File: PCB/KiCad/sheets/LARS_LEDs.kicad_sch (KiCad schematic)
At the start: 26 parts, among them J29 LED1, J30 LED2, SW2 User Button

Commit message: reannotate schematic
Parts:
- renumbered C66 to C68, C67 to C69, C68 to C70, J29 to J30, J30 to J31
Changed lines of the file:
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@@
 		(dnp no)
 		(fields_autoplaced yes)
-		(property "Reference" "#PWR0196"
+		(property "Reference" "#PWR0193"
 			(at 232.41 72.39 0)
 			(effects
@@
 			(project "hardware_interface"
 				(path "/ffedf44c-a51a-4124-b6d3-e3f1f256e9ac/1e19cc26-d5ec-4418-898d-5c13f17cd2aa"
-					(reference "#PWR0196")
+					(reference "#PWR0193")
 					(unit 1)
 				)
@@
 		(on_board yes)
 		(dnp no)
-		(property "Reference" "C68"
+		(property "Reference" "C70"
 			(at 150.114 137.922 0)
 			(effects
@@
 			(project "hardware_interface"
 				(path "/ffedf44c-a51a-4124-b6d3-e3f1f256e9ac/1e19cc26-d5ec-4418-898d-5c13f17cd2aa"
-					(reference "C68")
+					(reference "C70")
 					(unit 1)
 				)
@@
 		(on_board yes)
 		(dnp no)
-		(property "Reference" "C66"
+		(property "Reference" "C68"
 			(at 232.664 59.182 0)
 			(effects
@@
 			(project "hardware_interface"
 				(path "/ffedf44c-a51a-4124-b6d3-e3f1f256e9ac/1e19cc26-d5ec-4418-898d-5c13f17cd2aa"
-					(reference "C66")
+					(reference "C68")
 					(unit 1)
 				)
@@
 		(dnp no)
 		(fields_autoplaced yes)
-		(property "Reference" "#PWR0189"
+		(property "Reference" "#PWR0186"
 			(at 106.68 50.8 0)
 			(effects
@@
 			(project "hardware_interface"
 				(path "/ffedf44c-a51a-4124-b6d3-e3f1f256e9ac/1e19cc26-d5ec-4418-898d-5c13f17cd2aa"
-					(reference "#PWR0189")
+					(reference "#PWR0186")
 					(unit 1)
 				)
@@
 		(dnp no)
 		(fields_autoplaced yes)
-		(property "Reference" "#PWR0199"
+		(property "Reference" "#PWR0196"
 			(at 137.16 73.66 0)
 			(effects
@@
 			(project "hardware_interface"
 				(path "/ffedf44c-a51a-4124-b6d3-e3f1f256e9ac/1e19cc26-d5ec-4418-898d-5c13f17cd2aa"
-					(reference "#PWR0199")
+					(reference "#PWR0196")
 					(unit 1)
 				)
@@
 		(dnp no)
 		(fields_autoplaced yes)
-		(property "Reference" "#PWR0197"
+		(property "Reference" "#PWR0194"
 			(at 106.68 73.66 0)
 			(effects
@@
 			(project "hardware_interface"
 				(path "/ffedf44c-a51a-4124-b6d3-e3f1f256e9ac/1e19cc26-d5ec-4418-898d-5c13f17cd2aa"
-					(reference "#PWR0197")
+					(reference "#PWR0194")
 					(unit 1)
 				)
@@
 		(dnp no)
 		(fields_autoplaced yes)
-		(property "Reference" "#PWR0193"
+		(property "Reference" "#PWR0190"
 			(at 46.99 72.39 0)
 			(effects
@@
 			(project "hardware_interface"
 				(path "/ffedf44c-a51a-4124-b6d3-e3f1f256e9ac/1e19cc26-d5ec-4418-898d-5c13f17cd2aa"
-					(reference "#PWR0193")
+					(reference "#PWR0190")
 					(unit 1)
 				)
@@
 		(on_board yes)
 		(dnp no)
-		(property "Reference" "#PWR0205"
+		(property "Reference" "#PWR0202"
 			(at 143.51 133.35 0)
 			(effects
@@
 			(project "hardware_interface"
 				(path "/ffedf44c-a51a-4124-b6d3-e3f1f256e9ac/1e19cc26-d5ec-4418-898d-5c13f17cd2aa"
-					(reference "#PWR0205")
+					(reference "#PWR0202")
 					(unit 1)
 				)
@@
 		(on_board yes)
 		(dnp no)
-		(property "Reference" "C67"
+		(property "Reference" "C69"
 			(at 143.764 137.922 0)
 			(effects
@@
 			(project "hardware_interface"
 				(path "/ffedf44c-a51a-4124-b6d3-e3f1f256e9ac/1e19cc26-d5ec-4418-898d-5c13f17cd2aa"
-					(reference "C67")
+					(reference "C69")
 					(unit 1)
 				)
@@
 		(on_board yes)
 		(dnp no)
-		(property "Reference" "J30"
+		(property "Reference" "J31"
 			(at 120.142 134.366 0)
 			(effects
@@
 			(project "hardware_interface"
 				(path "/ffedf44c-a51a-4124-b6d3-e3f1f256e9ac/1e19cc26-d5ec-4418-898d-5c13f17cd2aa"
-					(reference "J30")
+					(reference "J31")
 					(unit 1)
 				)
@@
 		(on_board yes)
 		(dnp no)
-		(property "Reference" "J29"
+		(property "Reference" "J30"
 			(at 66.802 134.366 0)
 			(effects
@@
 			(project "hardware_interface"
 				(path "/ffedf44c-a51a-4124-b6d3-e3f1f256e9ac/1e19cc26-d5ec-4418-898d-5c13f17cd2aa"
-					(reference "J29")
+					(reference "J30")
 					(unit 1)
 				)
@@
 		(dnp no)
 		(fields_autoplaced yes)
-		(property "Reference" "#PWR0210"
+		(property "Reference" "#PWR0207"
 			(at 143.51 157.48 0)
 			(effects
@@
 			(project "hardware_interface"
 				(path "/ffedf44c-a51a-4124-b6d3-e3f1f256e9ac/1e19cc26-d5ec-4418-898d-5c13f17cd2aa"
-					(reference "#PWR0210")
+					(reference "#PWR0207")
 					(unit 1)
 				)
@@
 		(dnp no)
 		(fields_autoplaced yes)
-		(property "Reference" "#PWR0203"
+		(property "Reference" "#PWR0200"
 			(at 62.23 133.35 0)
 			(effects
@@
 			(project "hardware_interface"
 				(path "/ffedf44c-a51a-4124-b6d3-e3f1f256e9ac/1e19cc26-d5ec-4418-898d-5c13f17cd2aa"
-					(reference "#PWR0203")
+					(reference "#PWR0200")
 					(unit 1)
 				)
@@
 		(dnp no)
 		(fields_autoplaced yes)
-		(property "Reference" "#PWR0188"
+		(property "Reference" "#PWR0185"
 			(at 232.41 43.18 0)
 			(effects
@@
 			(project "hardware_interface"
 				(path "/ffedf44c-a51a-4124-b6d3-e3f1f256e9ac/1e19cc26-d5ec-4418-898d-5c13f17cd2aa"
-					(reference "#PWR0188")
+					(reference "#PWR0185")
 					(unit 1)
 				)
@@
 		(dnp no)
 		(fields_autoplaced yes)
-		(property "Reference" "#PWR0202"
+		(property "Reference" "#PWR0199"
 			(at 99.06 123.19 0)
 			(effects
@@
 			(project "hardware_interface"
 				(path "/ffedf44c-a51a-4124-b6d3-e3f1f256e9ac/1e19cc26-d5ec-4418-898d-5c13f17cd2aa"
-					(reference "#PWR0202")
+					(reference "#PWR0199")
 					(unit 1)
 				)
@@
 		(dnp no)
 		(fields_autoplaced yes)
-		(property "Reference" "#PWR0200"
+		(property "Reference" "#PWR0197"
 			(at 196.85 73.66 0)
 			(effects
@@
 			(project "hardware_interface"
 				(path "/ffedf44c-a51a-4124-b6d3-e3f1f256e9ac/1e19cc26-d5ec-4418-898d-5c13f17cd2aa"
-					(reference "#PWR0200")
+					(reference "#PWR0197")
 					(unit 1)
 				)
@@
 		(dnp no)
 		(fields_autoplaced yes)
-		(property "Reference" "#PWR0195"
+		(property "Reference" "#PWR0192"
 			(at 67.31 72.39 0)
 			(effects
@@
 			(project "hardware_interface"
 				(path "/ffedf44c-a51a-4124-b6d3-e3f1f256e9ac/1e19cc26-d5ec-4418-898d-5c13f17cd2aa"
-					(reference "#PWR0195")
+					(reference "#PWR0192")
 					(unit 1)
 				)
@@
 		(dnp no)
 		(fields_autoplaced yes)
-		(property "Reference" "#PWR0198"
+		(property "Reference" "#PWR0195"
 			(at 121.92 73.66 0)
 			(effects
@@
 			(project "hardware_interface"
 				(path "/ffedf44c-a51a-4124-b6d3-e3f1f256e9ac/1e19cc26-d5ec-4418-898d-5c13f17cd2aa"
-					(reference "#PWR0198")
+					(reference "#PWR0195")
 					(unit 1)
 				)
@@
 		(dnp no)
 		(fields_autoplaced yes)
-		(property "Reference" "#PWR0204"
+		(property "Reference" "#PWR0201"
 			(at 115.57 133.35 0)
 			(effects
@@
 			(project "hardware_interface"
 				(path "/ffedf44c-a51a-4124-b6d3-e3f1f256e9ac/1e19cc26-d5ec-4418-898d-5c13f17cd2aa"
-					(reference "#PWR0204")
+					(reference "#PWR0201")
 					(unit 1)
 				)
@@
 		(dnp no)
 		(fields_autoplaced yes)
-		(property "Reference" "#PWR0201"
+		(property "Reference" "#PWR0198"
 			(at 45.72 123.19 0)
 			(effects
@@
 			(project "hardware_interface"
 				(path "/ffedf44c-a51a-4124-b6d3-e3f1f256e9ac/1e19cc26-d5ec-4418-898d-5c13f17cd2aa"
-					(reference "#PWR0201")
+					(reference "#PWR0198")
 					(unit 1)
 				)
@@
 		(dnp no)
 		(fields_autoplaced yes)
-		(property "Reference" "#PWR0191"
+		(property "Reference" "#PWR0188"
 			(at 137.16 50.8 0)
 			(effects
@@
 			(project "hardware_interface"
 				(path "/ffedf44c-a51a-4124-b6d3-e3f1f256e9ac/1e19cc26-d5ec-4418-898d-5c13f17cd2aa"
-					(reference "#PWR0191")
+					(reference "#PWR0188")
 					(unit 1)
 				)
@@
 		(dnp no)
 		(fields_autoplaced yes)
-		(property "Reference" "#PWR0194"
+		(property "Reference" "#PWR0191"
 			(at 57.15 72.39 0)
 			(effects
@@
 			(project "hardware_interface"
 				(path "/ffedf44c-a51a-4124-b6d3-e3f1f256e9ac/1e19cc26-d5ec-4418-898d-5c13f17cd2aa"
-					(reference "#PWR0194")
+					(reference "#PWR0191")
 					(unit 1)
 				)
@@
 		(dnp no)
 		(fields_autoplaced yes)
-		(property "Reference" "#PWR0208"
+		(property "Reference" "#PWR0205"
 			(at 99.06 157.48 0)
 			(effects
@@
 			(project "hardware_interface"
 				(path "/ffedf44c-a51a-4124-b6d3-e3f1f256e9ac/1e19cc26-d5ec-4418-898d-5c13f17cd2aa"
-					(reference "#PWR0208")
+					(reference "#PWR0205")
 					(unit 1)
 				)
@@
 		(dnp no)
 		(fields_autoplaced yes)
-		(property "Reference" "#PWR0206"
+		(property "Reference" "#PWR0203"
 			(at 45.72 157.48 0)
 			(effects
@@
 			(project "hardware_interface"
 				(path "/ffedf44c-a51a-4124-b6d3-e3f1f256e9ac/1e19cc26-d5ec-4418-898d-5c13f17cd2aa"
-					(reference "#PWR0206")
+					(reference "#PWR0203")
 					(unit 1)
 				)
@@
 		(dnp no)
 		(fields_autoplaced yes)
-		(property "Reference" "#PWR0192"
+		(property "Reference" "#PWR0189"
 			(at 158.75 50.8 0)
 			(effects
@@
 			(project "hardware_interface"
 				(path "/ffedf44c-a51a-4124-b6d3-e3f1f256e9ac/1e19cc26-d5ec-4418-898d-5c13f17cd2aa"
-					(reference "#PWR0192")
+					(reference "#PWR0189")
 					(unit 1)
 				)
@@
 		(dnp no)
 		(fields_autoplaced yes)
-		(property "Reference" "#PWR0209"
+		(property "Reference" "#PWR0206"
 			(at 115.57 157.48 0)
 			(effects
@@
 			(project "hardware_interface"
 				(path "/ffedf44c-a51a-4124-b6d3-e3f1f256e9ac/1e19cc26-d5ec-4418-898d-5c13f17cd2aa"
-					(reference "#PWR0209")
+					(reference "#PWR0206")
 					(unit 1)
 				)
@@
 		(dnp no)
 		(fields_autoplaced yes)
-		(property "Reference" "#PWR0207"
+		(property "Reference" "#PWR0204"
 			(at 62.23 157.48 0)
 			(effects
@@
 			(project "hardware_interface"
 				(path "/ffedf44c-a51a-4124-b6d3-e3f1f256e9ac/1e19cc26-d5ec-4418-898d-5c13f17cd2aa"
-					(reference "#PWR0207")
+					(reference "#PWR0204")
 					(unit 1)
 				)
@@
 		(on_board yes)
 		(dnp no)
-		(property "Reference" "#PWR0190"
+		(property "Reference" "#PWR0187"
 			(at 121.92 50.8 0)
 			(effects
@@
 			(project "hardware_interface"
 				(path "/ffedf44c-a51a-4124-b6d3-e3f1f256e9ac/1e19cc26-d5ec-4418-898d-5c13f17cd2aa"
-					(reference "#PWR0190")
+					(reference "#PWR0187")
 					(unit 1)
 				)

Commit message: add final traces
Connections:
- net +5V: no longer D16.2 (A), D17.2 (A)
- net +5V_OUT: now also D16.2 (A), D17.2 (A)
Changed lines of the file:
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@@
 			)
 		)
-		(property "Value" "+5V"
+		(property "Value" "+5V_OUT"
 			(at 99.06 114.3 0)
 			(effects
@@
 			)
 		)
-		(property "Value" "+5V"
+		(property "Value" "+5V_OUT"
 			(at 45.72 114.3 0)
 			(effects

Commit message: finish PCB routing
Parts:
- C68: value 1u -> 2u2
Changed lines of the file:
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@@
 			)
 		)
-		(property "Value" "1u"
+		(property "Value" "2u2"
 			(at 232.918 62.992 0)
 			(effects

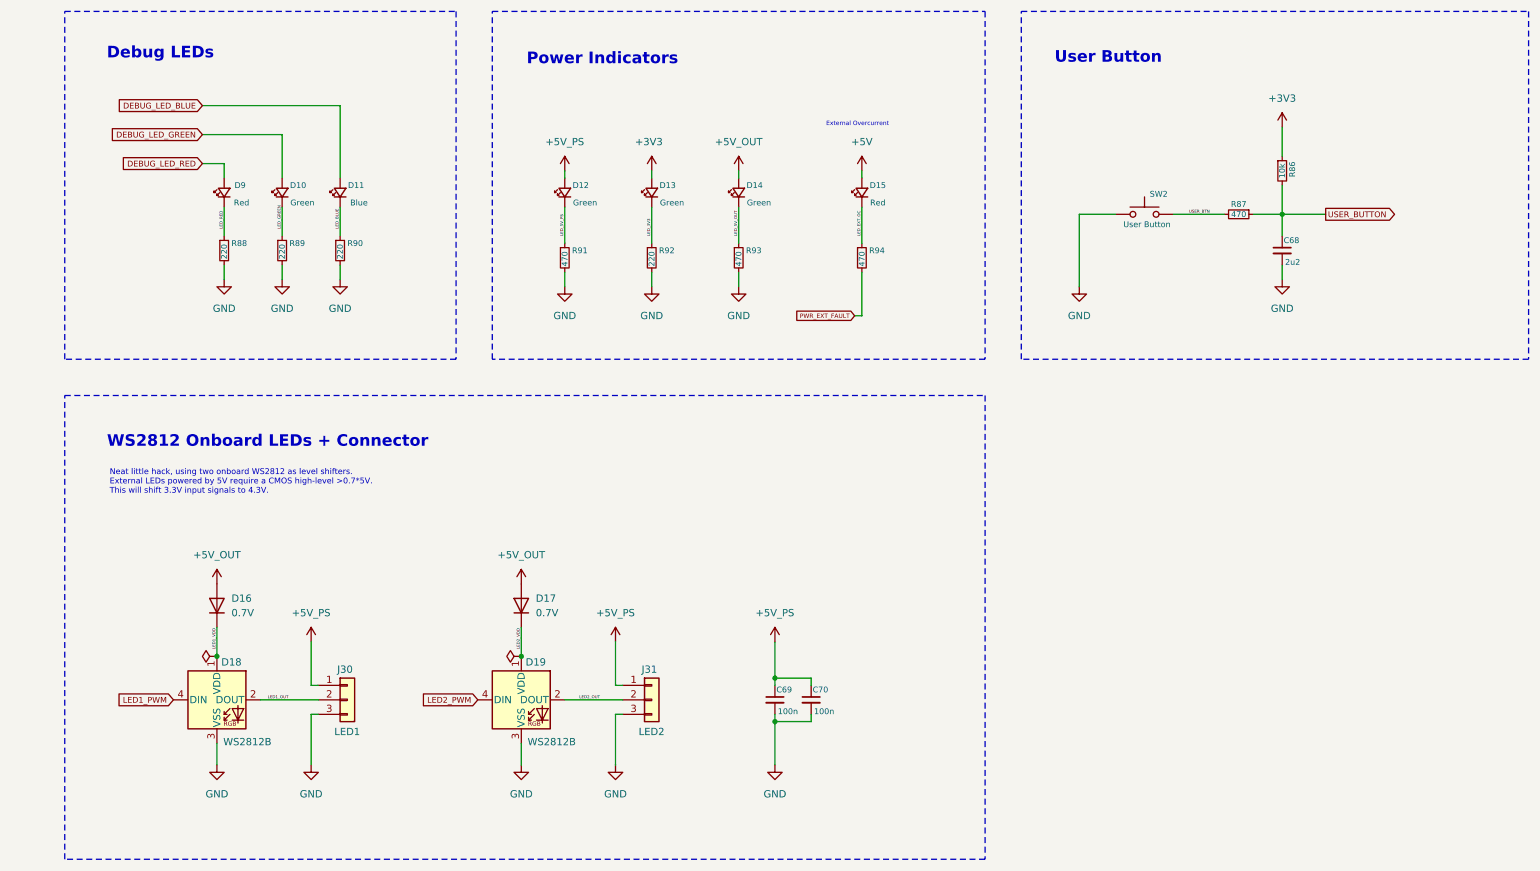
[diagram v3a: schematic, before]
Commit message: change default KiCad schematic font
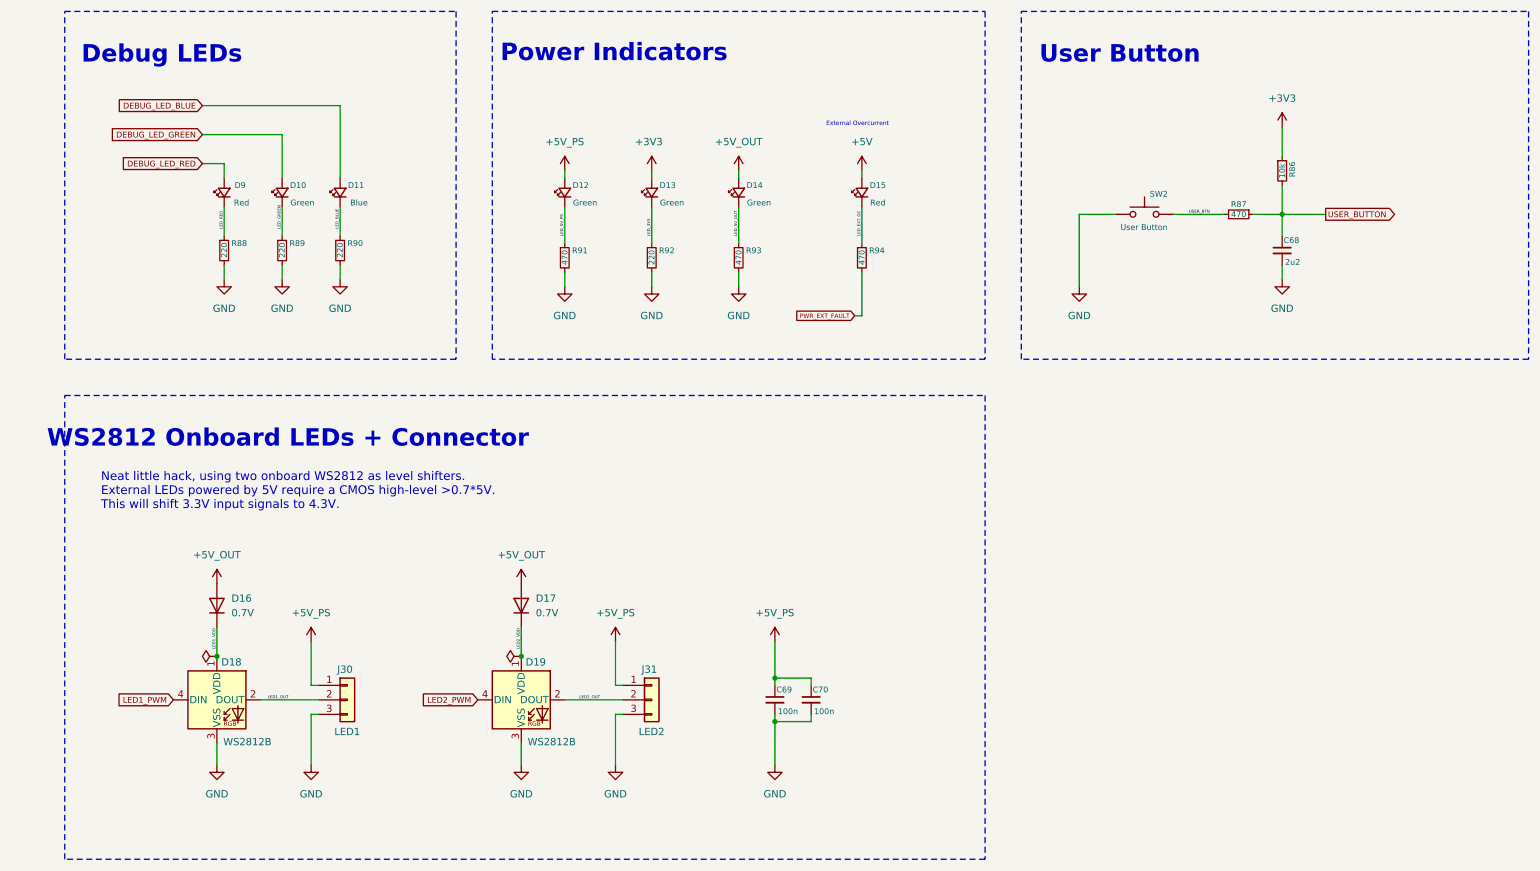
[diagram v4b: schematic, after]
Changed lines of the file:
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@@
 	(text "WS2812 Onboard LEDs + Connector"
 		(exclude_from_sim no)
-		(at 54.61 94.488 0)
+		(at 58.166 93.98 0)
 		(effects
 			(font
-				(size 2.032 2.032)
+				(size 3.048 3.048)
 				(thickness 0.4064)
 				(bold yes)
@@
 	(text "Power Indicators"
 		(exclude_from_sim no)
-		(at 113.284 27.432 0)
+		(at 115.316 26.416 0)
 		(effects
 			(font
-				(size 2.032 2.032)
+				(size 3.048 3.048)
 				(thickness 0.4064)
 				(bold yes)
@@
 	(text "User Button"
 		(exclude_from_sim no)
-		(at 201.93 27.178 0)
+		(at 203.962 26.67 0)
 		(effects
 			(font
-				(size 2.032 2.032)
+				(size 3.048 3.048)
 				(thickness 0.4064)
 				(bold yes)
@@
 	(text "Debug LEDs"
 		(exclude_from_sim no)
-		(at 35.814 26.416 0)
+		(at 36.068 26.67 0)
 		(effects
 			(font
-				(size 2.032 2.032)
+				(size 3.048 3.048)
 				(thickness 0.4064)
 				(bold yes)
@@
 	(text "Neat little hack, using two onboard WS2812 as level shifters.\nExternal LEDs powered by 5V require a CMOS high-level >0.7*5V.\nThis will shift 3.3V input signals to 4.3V.\n "
 		(exclude_from_sim no)
-		(at 26.924 102.362 0)
+		(at 25.4 104.394 0)
 		(effects
 			(font
-				(size 1.016 1.016)
+				(size 1.524 1.524)
 			)
 			(justify left)
@@
 		)
 		(property "Value" "470"
-			(at 158.75 63.754 90)
+			(at 158.75 63.5 90)
 			(effects
 				(font
@@
 		)
 		(property "Value" "470"
-			(at 106.68 63.754 90)
+			(at 106.68 63.5 90)
 			(effects
 				(font
@@
 		)
 		(property "Value" "220"
-			(at 46.99 62.484 90)
+			(at 46.99 62.23 90)
 			(effects
 				(font
@@
 		)
 		(property "Value" "220"
-			(at 121.92 63.754 90)
+			(at 121.92 63.5 90)
 			(effects
 				(font
@@
 		)
 		(property "Value" "220"
-			(at 57.15 62.484 90)
+			(at 57.15 62.23 90)
 			(effects
 				(font
@@
 		)
 		(property "Value" "User Button"
-			(at 212.852 56.388 0)
+			(at 212.344 56.896 0)
 			(effects
 				(font
@@
 		)
 		(property "Value" "220"
-			(at 67.31 62.484 90)
+			(at 67.31 62.23 90)
 			(effects
 				(font
@@
 		)
 		(property "Value" "470"
-			(at 137.16 63.754 90)
+			(at 137.16 63.5 90)
 			(effects
 				(font

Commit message: update text layout and fix remaining DRC errors
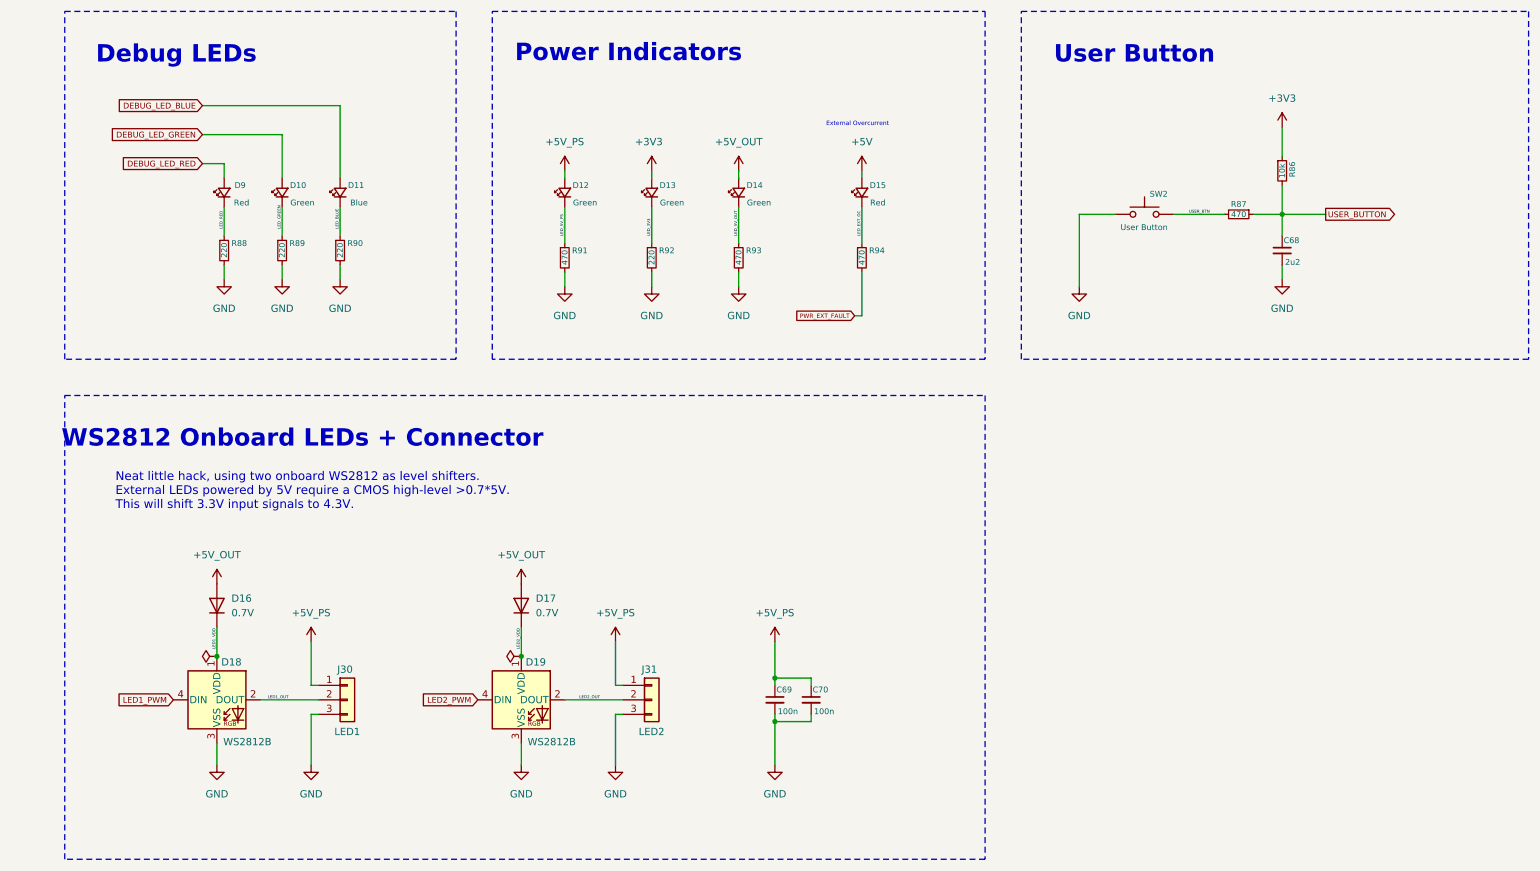
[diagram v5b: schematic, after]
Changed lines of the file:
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@@
 	(text "WS2812 Onboard LEDs + Connector"
 		(exclude_from_sim no)
-		(at 58.166 93.98 0)
+		(at 60.706 93.98 0)
 		(effects
 			(font
@@
 	(text "Power Indicators"
 		(exclude_from_sim no)
-		(at 115.316 26.416 0)
+		(at 117.856 26.416 0)
 		(effects
 			(font
@@
 	(text "User Button"
 		(exclude_from_sim no)
-		(at 203.962 26.67 0)
+		(at 206.502 26.67 0)
 		(effects
 			(font
@@
 	(text "Debug LEDs"
 		(exclude_from_sim no)
-		(at 36.068 26.67 0)
+		(at 38.608 26.67 0)
 		(effects
 			(font
@@
 	(text "Neat little hack, using two onboard WS2812 as level shifters.\nExternal LEDs powered by 5V require a CMOS high-level >0.7*5V.\nThis will shift 3.3V input signals to 4.3V.\n "
 		(exclude_from_sim no)
-		(at 25.4 104.394 0)
+		(at 27.94 104.394 0)
 		(effects
 			(font
